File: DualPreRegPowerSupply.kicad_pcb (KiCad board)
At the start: 4 copper layers, 100 x 100 mm, 338 parts, among them J101 Power Input, J102 Conn_01x03_Pin, J103 Conn_02x02_Odd_Even, J201 Banana_Red, J202 Banana_Black, J401 Conn_02x05_Odd_Even, J402 Banana_Red, J403 Banana_Black, J601 Power Input, J801 Conn_01x03_Pin, J802 Conn_02x02_Odd_Even, J901 Power Input, M401 Fan_4pin, Q101 MMBT3906, Q102 BCP56, Q103 BSS138, Q104 TIP125, Q105 BSS138, Q106 BSS138, Q107 BCP56, Q301 BCP56, Q302 BSS138, Q303 TIP125, Q304 BCP56, Q401 BSS138, Q501 MMBT3906, Q801 BSS138, Q802 BSS138, U1002 AP7383, U1003 LM2776, U1004 XC6901D121MR-G, U101 TLV4387PWR, U102 ISO6721RFBD, U104 LT8612, U105 LMV331, U106 ATtiny1614-SS, U107 ADS1118IDGS, U108 MCP48FVB22, U109 AP7383, U110 LM2776, U111 XC6901D121MR-G, U1501 LMR51606, U301 TLV4387PWR, U302 LMV331, U401 TMP1075D, U501 LT8612, U601 LMR51606, U701 ADS1118IDGS, U702 MCP48FVB22, U801 ISO6721RFBD, U802 ATtiny1614-SS, U901 AP63200WU

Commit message: add adc and dac estimate
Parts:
- removed BZ401: Buzzer, Buzzer_Beeper:Buzzer_12x9.5RM7.6
- removed C403: 100n, Capacitor_SMD:C_0603_1608Metric
- removed Q401: BSS138, Package_TO_SOT_SMD:SOT-23-3
- removed R201: 10k, Resistor_SMD:R_0603_1608Metric
- removed R403: 1k, Resistor_SMD:R_0603_1608Metric
- added C202: 10u, Capacitor_SMD:C_0805_2012Metric, B.Cu at (140.5, 133.4)
- added J204: Conn_02x05_Odd_Even, Connector_IDC:IDC-Header_2x05_P2.54mm_Vertical, B.Cu at (155.1, 77.4)
- moved TP1501 80.7 mm to (228.0, 60.9)
- moved TP1502 80.7 mm to (228.0, 55.8)
- moved TP1503 80.7 mm to (218.5, 62.6)
- moved TP1504 80.7 mm to (218.5, 59.3)
- moved TP1505 80.7 mm to (218.5, 56.0)
- moved TP1506 80.7 mm to (222.5, 62.7)
- moved D903 23.0 mm to (156.8, 59.9)
- moved R904 23.0 mm to (156.8, 56.8)
- moved D902 22.3 mm to (153.1, 59.9)
- moved R901 22.3 mm to (153.1, 56.8)
- moved TP110 12.5 mm to (184.1, 78.7)
- moved R202 6.65 mm to (157.2, 52.4)
- moved R404 6.65 mm to (158.8, 52.4)
- moved C404 5.82 mm to (152.5, 51.6)
- moved F901 4.52 mm to (141.7, 52.9), turned to 180 degrees
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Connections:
- A401 pad 16: unconnected-(A401-GPIO16/LED-Pad16) -> /Control/W5500_MISO
- A401 pad 18: unconnected-(A401-GPIO18-Pad18) -> /Control/W5500_SCLK
- A401 pad 19: unconnected-(A401-GPIO19-Pad19) -> /Control/W5500_MOSI
- A401 pad 20: unconnected-(A401-GPIO20-Pad20) -> /Control/W5500_CS
- A401 pad 21: unconnected-(A401-GPIO21-Pad21) -> /Control/W5500_RST
- A401 pad 22: unconnected-(A401-GPIO22-Pad22) -> /Control/W5500_INT
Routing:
- net /Control/W5500_MOSI: track 0.00 -> 43.0 mm
- net /Control/W5500_SCLK: track 0.00 -> 41.1 mm
- net /Control/W5500_CS: track 0.00 -> 40.3 mm
- net /Control/W5500_RST: track 0.00 -> 36.7 mm
- net /Control/W5500_INT: track 0.00 -> 36.7 mm
- net /Control/W5500_MISO: track 0.00 -> 33.0 mm
- net /Control/Buzzer: track 32.3 -> 0.00 mm
- net /Control/FanPWM: track 58.2 -> 65.4 mm
- net +12V: track 32.6 -> 26.9 mm
- net Net-(BZ401--): track 5.10 -> 0.00 mm
- net Net-(M401-PWM): track 5.92 -> 2.30 mm
- net Net-(J901-Pin_2): track 6.42 -> 4.09 mm
- net Net-(Q401-G): track 1.96 -> 0.00 mm
- net /Control/RESET: track 23.0 -> 23.8 mm
- net /Ch1Power/Rx_Ctr: track 14.9 -> 14.1 mm
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
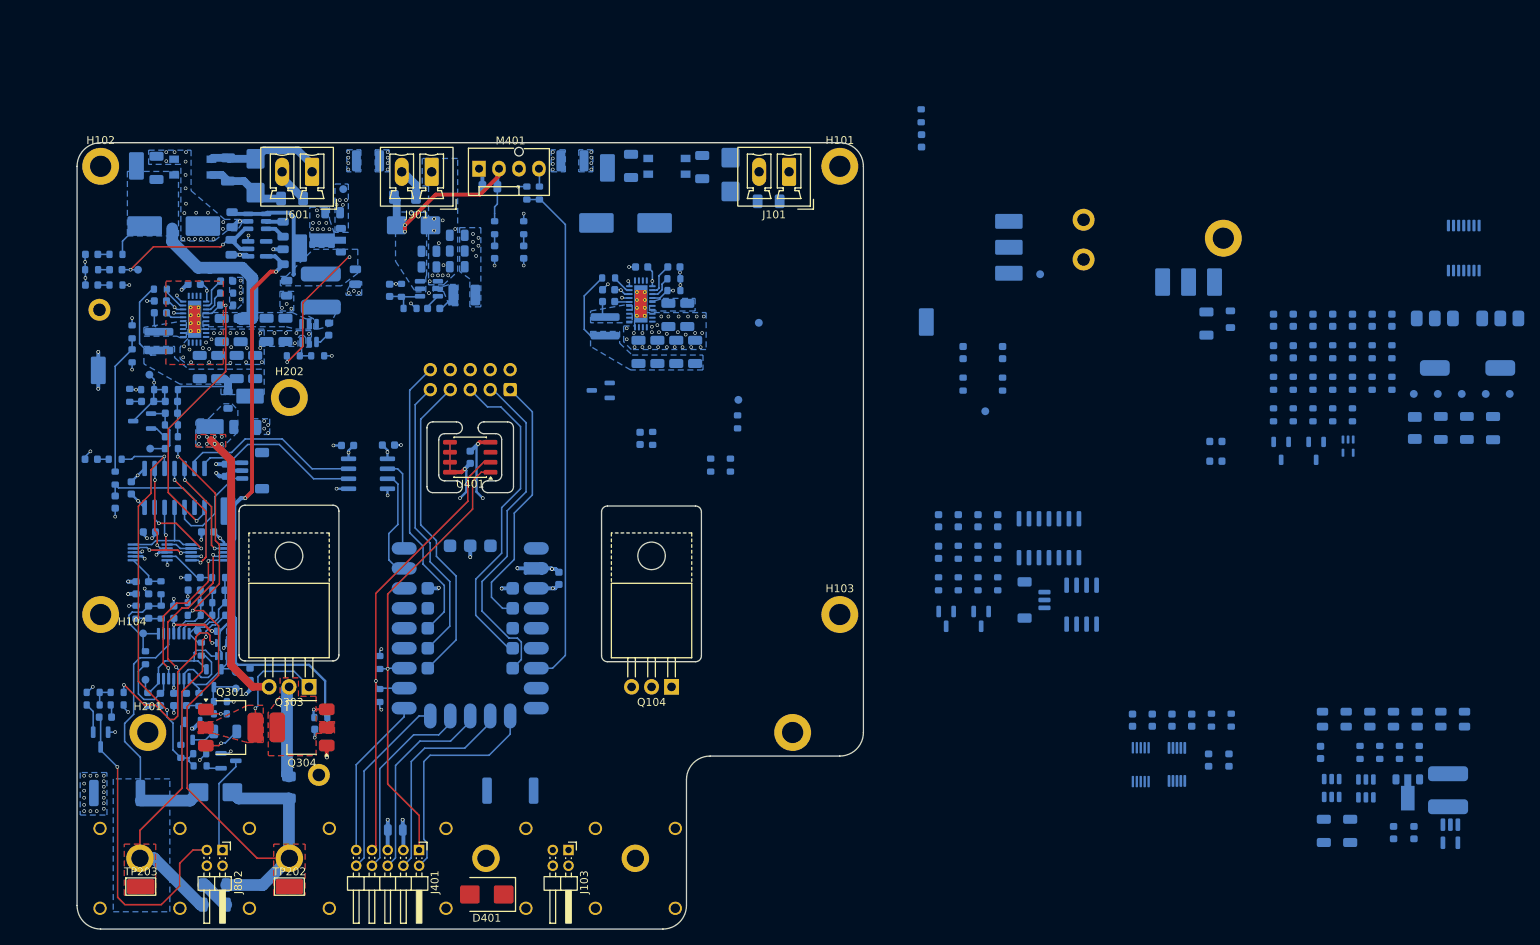
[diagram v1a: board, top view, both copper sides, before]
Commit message: add diodes for clamping
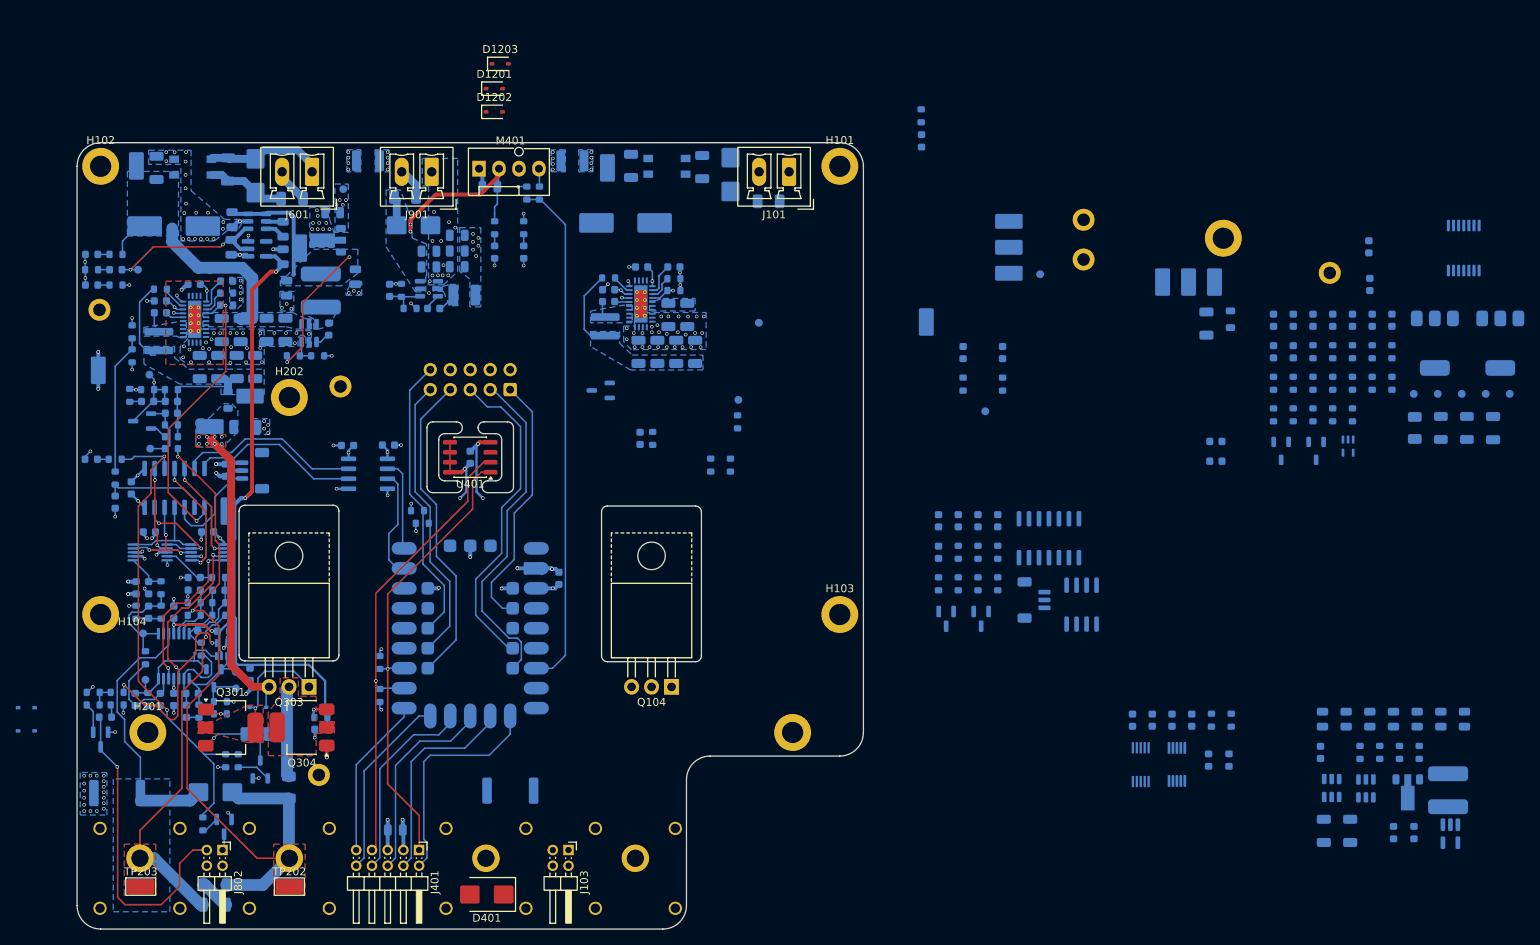
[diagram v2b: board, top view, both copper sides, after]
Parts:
- added C1004: 100p, Capacitor_SMD:C_0603_1608Metric, B.Cu at (107.4, 116.8)
- added C1014: 100p, Capacitor_SMD:C_0603_1608Metric, B.Cu at (114.6, 116.0)
- added C1203: 100p, Capacitor_SMD:C_0603_1608Metric, B.Cu at (264.4, 64.0)
- added C1204: 100p, Capacitor_SMD:C_0603_1608Metric, B.Cu at (264.3, 59.2)
- added D1003: 1N4148WS, Diode_SMD:D_SOD-323, B.Cu at (93.5, 117.8)
- added D1004: 1N4148WS, Diode_SMD:D_SOD-323, B.Cu at (93.5, 120.8)
- added D1005: MM3Z4V7T1G, Diode_SMD:D_SOD-323, B.Cu at (123.0, 117.8)
- added D1201: 1N4148WS, Diode_SMD:D_SOD-323, F.Cu at (153.1, 39.1)
- added D1202: 1N4148WS, Diode_SMD:D_SOD-323, F.Cu at (153.1, 42.1)
- added D1203: MM3Z4V7T1G, Diode_SMD:D_SOD-323, F.Cu at (153.8, 36.0)
- added R201: 2k, Resistor_SMD:R_0603_1608Metric, B.Cu at (143.3, 92.8)
- added R203: 2k, Resistor_SMD:R_0603_1608Metric, B.Cu at (143.9, 94.4)
- added TP1507: TestPoint_Alt, TestPoint:TestPoint_Keystone_5005-5009_Compact, B.Cu at (259.3, 62.6)
- added TP602: TestPoint_Alt, TestPoint:TestPoint_Keystone_5005-5009_Compact, B.Cu at (133.5, 77.0)
- moved Q302 9.90 mm to (123.3, 125.7), turned to 90 degrees
- moved Q801 8.42 mm to (118.7, 133.0), turned to -90 degrees
- moved R312 7.40 mm to (120.5, 124.6), turned to 90 degrees
- moved R804 7.38 mm to (116.0, 132.6), turned to -90 degrees
- moved R315 3.96 mm to (122.8, 121.2), turned to 0 degrees
- moved R310 3.42 mm to (118.9, 124.6), turned to 90 degrees
- moved C303 1.50 mm to (113.9, 118.3)
- moved R303 1.50 mm to (115.5, 118.3)
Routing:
- net /Ch1Power/Linear_PostReg/OE: track 52.1 -> 63.3 mm
- net /Ch1Power/MCU/~{LED_Enable}: track 12.4 -> 2.73 mm
- net /Ch1Power/Linear_PostReg/PreReg: track 35.6 -> 38.4 mm
- net Net-(D1003-K): track 9.59 -> 12.3 mm
- net +3.3V: track 26.1 -> 28.0 mm, vias 16 -> 18
- net /Ch1Power/Linear_PostReg/CC_loop: track 17.2 -> 18.9 mm
- net Net-(D1004-K): track 10.1 -> 11.6 mm
- net /Ch1Power/Linear_PostReg/CV_loop: track 11.5 -> 13.0 mm
- net Net-(Q302-G): track 3.14 -> 4.34 mm
- net GND_Ch1: track 49.4 -> 48.3 mm
- net Net-(Q301-E): track 4.68 -> 5.57 mm
- net /Ch1Power/Linear_PostReg/OUT-: track 78.5 -> 79.3 mm
- net /Ch1Power/Linear_PostReg/Base_drive: track 14.2 -> 14.9 mm
- net Net-(Q302-D): track 3.13 -> 3.76 mm
